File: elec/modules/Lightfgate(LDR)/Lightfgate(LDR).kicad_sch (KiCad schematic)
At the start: 2 parts, among them J1 Conn_01x02

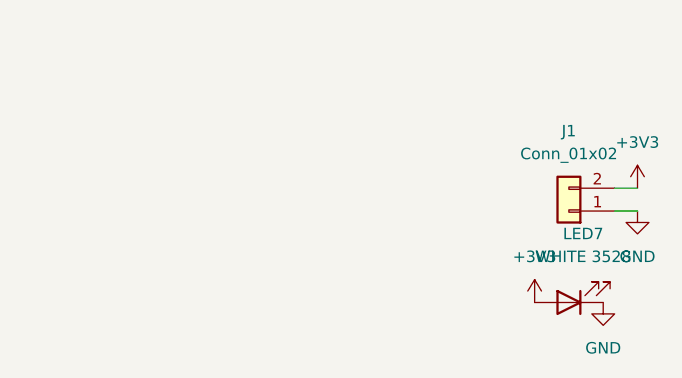
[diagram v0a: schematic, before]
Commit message: added ldr folder
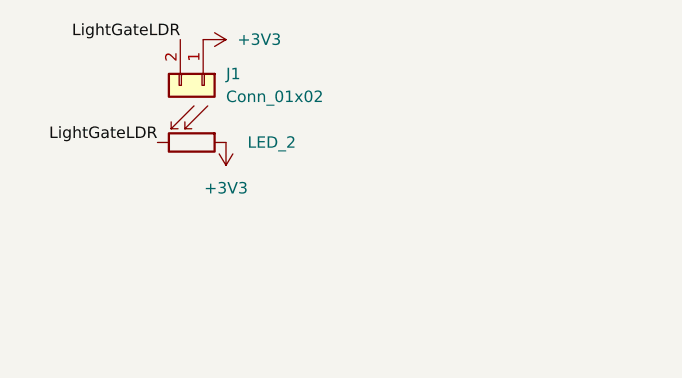
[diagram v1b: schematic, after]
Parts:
- removed LED7: WHITE 3528, LED_SMD:LED_PLCC_2835, symbol Device:LED
- added LED_2: R_Photo, Resistor_SMD:R_0603_1608Metric, symbol Device:R_Photo
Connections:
- net GND is gone; now on net +3V3: J1.1 (Pin_1)
- net +3V3: now also LED_2.1; no longer J1.2 (Pin_2)
- new net LightGateLDR: J1.2 (Pin_2), LED_2.2

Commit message: idk
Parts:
- J1: footprint Pinheaders:PinHeader_1x02_P2.54mm_Vertical -> Connector_JST:JST_SH_BM02B-SRSS-TB_1x02-1MP_P1.00mm_Vertical
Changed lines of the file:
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@@
 			)
 		)
-		(property "Footprint" "Pinheaders:PinHeader_1x02_P2.54mm_Vertical"
+		(property "Footprint" "Connector_JST:JST_SH_BM02B-SRSS-TB_1x02-1MP_P1.00mm_Vertical"
 			(at 80.01 86.36 0)
 			(effects
